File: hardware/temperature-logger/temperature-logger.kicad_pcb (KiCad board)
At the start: 2 copper layers, 40 x 30 mm, 20 parts, among them J1 Conn_01x05, U1 ATtiny85-20SU, U2 NCP1117-5.0_TO252, U3 MCP9801, U4 DS1307ZN+, U5 24FC512, Y1 Crystal

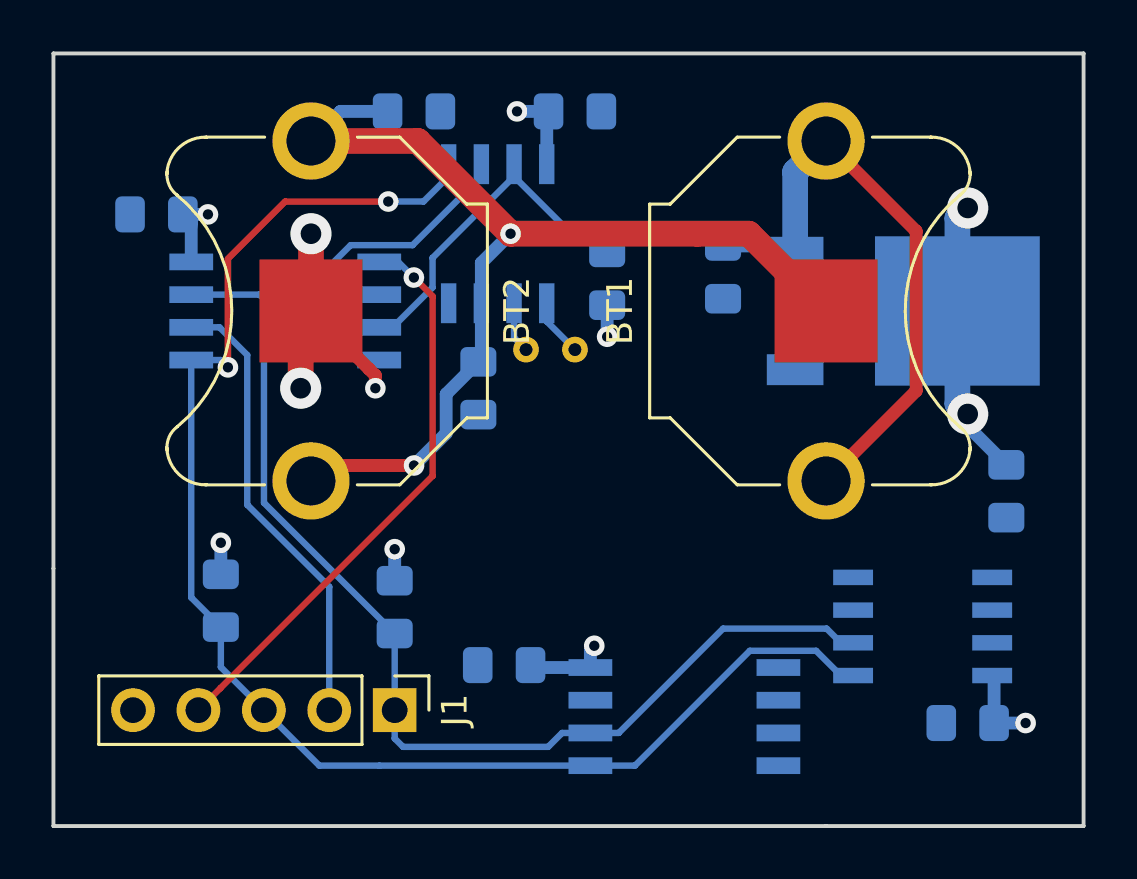
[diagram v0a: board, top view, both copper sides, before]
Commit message: create gerbers for jlc
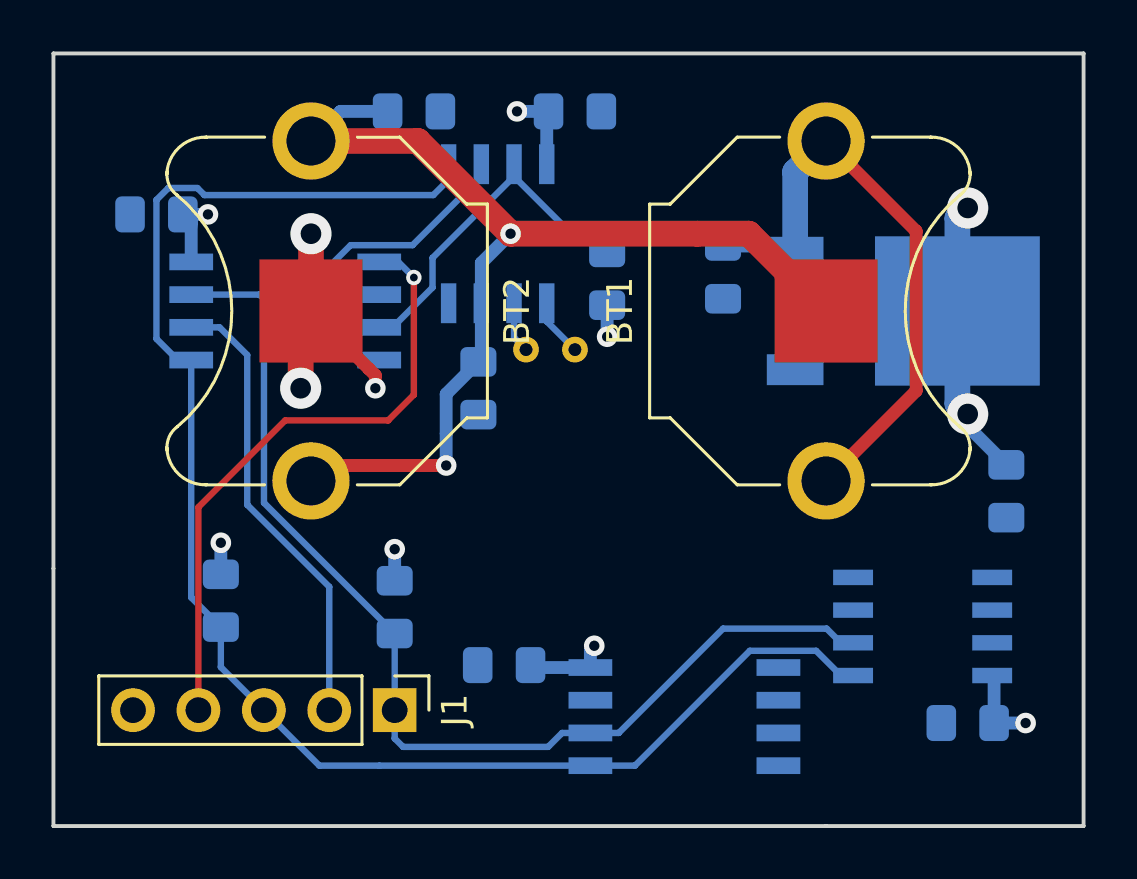
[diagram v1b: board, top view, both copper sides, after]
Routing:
- net /SDA: track 57.1 -> 60.6 mm, vias 2 -> 0
- net /~RESET: track 22.5 -> 24.6 mm
- net +BATT: track 41.0 -> 41.7 mm
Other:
- net class Default: via_dia 0.8 -> 0.6; via_drill 0.4 -> 0.3
- rule via_min_size: 0.4 -> 0.5
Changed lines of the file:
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@@
     (thickness 1.6)
     (drawings 6)
-    (tracks 135)
+    (tracks 136)
     (zones 0)
     (modules 20)
@@
   )
   (setup
-    (last_trace_width 0.25)
+    (last_trace_width 0.5)
     (user_trace_width 0.5)
     (user_trace_width 1)
@@
     (segment_width 0.2)
     (edge_width 0.15)
-    (via_size 0.8)
-    (via_drill 0.4)
-    (via_min_size 0.4)
+    (via_size 0.6)
+    (via_drill 0.3)
+    (via_min_size 0.5)
     (via_min_drill 0.3)
+    (user_via 0.8 0.4)
     (user_via 1.6 0.8)
     (uvia_size 0.3)
@@
     (visible_elements 7FFFFFFF)
     (pcbplotparams
-      (layerselection 0x010fc_ffffffff)
+      (layerselection 0x010f0_ffffffff)
       (usegerberextensions false)
-      (usegerberattributes false)
+      (usegerberattributes true)
       (usegerberadvancedattributes false)
       (creategerberjobfile false)
-      (excludeedgelayer true)
+      (excludeedgelayer false)
       (linewidth 0.100000)
       (plotframeref false)
       (viasonmask false)
       (mode 1)
-      (useauxorigin false)
+      (useauxorigin true)
       (hpglpennumber 1)
       (hpglpenspeed 20)
@@
       (outputformat 1)
       (mirror false)
-      (drillshape 1)
+      (drillshape 0)
       (scaleselection 1)
-      (outputdirectory ""))
+      (outputdirectory "gerber/"))
   )
   (net 0 "")
@@
     (clearance 0.2)
     (trace_width 0.25)
-    (via_dia 0.8)
-    (via_drill 0.4)
+    (via_dia 0.6)
+    (via_drill 0.3)
     (uvia_dia 0.3)
     (uvia_drill 0.1)
@@
     (tags "resistor handsolder")
     (attr smd)
-    (fp_text reference R3 (at -2.75 -0.25 90) (layer B.SilkS)
+    (fp_text reference R3 (at -2.75 0.25 90) (layer B.SilkS)
       (effects (font (size 1 1) (thickness 0.15)) (justify mirror))
     )
@@
   (segment (start 96.615 89.7) (end 96.615 91.86) (width 0.5) (layer B.Cu) (net 1))
   (segment (start 96.5 91.975) (end 95.25 93.225) (width 0.5) (layer B.Cu) (net 1))
-  (via (at 94 96) (size 0.8) (drill 0.4) (layers F.Cu B.Cu) (net 1))
   (segment (start 95.25 93.225) (end 95.25 94.75) (width 0.5) (layer B.Cu) (net 1))
-  (segment (start 95.25 94.75) (end 94 96) (width 0.5) (layer B.Cu) (net 1))
   (segment (start 90.6 96) (end 90 96.6) (width 0.5) (layer F.Cu) (net 1))
   (segment (start 94 96) (end 90.6 96) (width 0.5) (layer F.Cu) (net 1))
+  (segment (start 95.25 94.75) (end 95.25 96) (width 0.5) (layer B.Cu) (net 1))
+  (segment (start 94 96) (end 95.25 96) (width 0.5) (layer F.Cu) (net 1))
+  (via (at 95.25 96) (size 0.8) (drill 0.4) (layers F.Cu B.Cu) (net 1))
   (segment (start 108.8 84.6) (end 110 83.4) (width 1) (layer B.Cu) (net 2))
   (segment (start 108.8 87.72) (end 108.8 84.6) (width 1) (layer B.Cu) (net 2))
@@
   (segment (start 107.039999 103.194999) (end 109.614999 103.194999) (width 0.25) (layer B.Cu) (net 7))
   (segment (start 92.655 107.655) (end 100.85 107.655) (width 0.25) (layer B.Cu) (net 7))
-  (via (at 93 85.75) (size 0.8) (drill 0.4) (layers F.Cu B.Cu) (net 7))
-  (segment (start 95.345 84.775) (end 95.345 84.3) (width 0.25) (layer B.Cu) (net 7))
-  (segment (start 94.37 85.75) (end 95.345 84.775) (width 0.25) (layer B.Cu) (net 7))
-  (segment (start 93 85.75) (end 94.37 85.75) (width 0.25) (layer B.Cu) (net 7))
-  (via (at 86.77499 92.188647) (size 0.8) (drill 0.4) (layers F.Cu B.Cu) (net 7))
-  (segment (start 86.77499 87.97501) (end 86.77499 91.622962) (width 0.25) (layer F.Cu) (net 7))
-  (segment (start 86.77499 91.622962) (end 86.77499 92.188647) (width 0.25) (layer F.Cu) (net 7))
-  (segment (start 89 85.75) (end 86.77499 87.97501) (width 0.25) (layer F.Cu) (net 7))
-  (segment (start 93 85.75) (end 89 85.75) (width 0.25) (layer F.Cu) (net 7))
-  (segment (start 85.35 91.905) (end 86.491343 91.905) (width 0.25) (layer B.Cu) (net 7))
-  (segment (start 86.491343 91.905) (end 86.77499 92.188647) (width 0.25) (layer B.Cu) (net 7))
   (segment (start 90.325 107.655) (end 92.655 107.655) (width 0.25) (layer B.Cu) (net 7))
   (segment (start 88.17 105.5) (end 90.325 107.655) (width 0.25) (layer B.Cu) (net 7))
-  (via (at 93.994989 88.700901) (size 0.8) (drill 0.4) (layers F.Cu B.Cu) (net 8))
+  (segment (start 84.825 91.905) (end 84 91.08) (width 0.25) (layer B.Cu) (net 7))
+  (segment (start 85.35 91.905) (end 84.825 91.905) (width 0.25) (layer B.Cu) (net 7))
+  (segment (start 84 91.08) (end 84 85.68681) (width 0.25) (layer B.Cu) (net 7))
+  (segment (start 84 85.68681) (end 84.46182 85.22499) (width 0.25) (layer B.Cu) (net 7))
+  (segment (start 95.345 84.3) (end 95.345 84.905) (width 0.25) (layer B.Cu) (net 7))
+  (segment (start 95.345 84.905) (end 94.75 85.5) (width 0.25) (layer B.Cu) (net 7))
+  (segment (start 85.58818 85.22499) (end 84.46182 85.22499) (width 0.25) (layer B.Cu) (net 7))
+  (segment (start 85.86319 85.5) (end 85.58818 85.22499) (width 0.25) (layer B.Cu) (net 7))
+  (segment (start 94.75 85.5) (end 85.86319 85.5) (width 0.25) (layer B.Cu) (net 7))
   (segment (start 92.65 88.095) (end 93.389088 88.095) (width 0.25) (layer B.Cu) (net 8))
   (segment (start 93.389088 88.095) (end 93.994989 88.700901) (width 0.25) (layer B.Cu) (net 8))
-  (segment (start 94.725002 89.430914) (end 94.725002 96.404998) (width 0.25) (layer F.Cu) (net 8))
-  (segment (start 86.479999 104.650001) (end 85.63 105.5) (width 0.25) (layer F.Cu) (net 8))
-  (segment (start 93.994989 88.700901) (end 94.725002 89.430914) (width 0.25) (layer F.Cu) (net 8))
-  (segment (start 94.725002 96.404998) (end 86.479999 104.650001) (width 0.25) (layer F.Cu) (net 8))
+  (via (at 93.994989 88.700901) (size 0.6) (drill 0.3) (layers F.Cu B.Cu) (net 8))
+  (segment (start 85.63 105.5) (end 85.63 105.12) (width 0.25) (layer F.Cu) (net 8))
+  (segment (start 85.63 105.5) (end 85.63 97.62) (width 0.25) (layer F.Cu) (net 8))
+  (segment (start 85.63 97.62) (end 89 94.25) (width 0.25) (layer F.Cu) (net 8))
+  (segment (start 89 94.25) (end 93 94.25) (width 0.25) (layer F.Cu) (net 8))
+  (segment (start 93.994989 93.255011) (end 93.994989 88.700901) (width 0.25) (layer F.Cu) (net 8))
+  (segment (start 93 94.25) (end 93.994989 93.255011) (width 0.25) (layer F.Cu) (net 8))
   (segment (start 97.885 84.775) (end 97.885 84.3) (width 0.25) (layer B.Cu) (net 9))
   (segment (start 100.211628 87.101628) (end 97.885 84.775) (width 0.25) (layer B.Cu) (net 9))
